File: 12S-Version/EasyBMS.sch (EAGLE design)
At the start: 146 parts, among them IC1 LTC6811IG-2#PBF, Q10 BSS84LT1G, Q11 BSS84LT1G, Q12 BSS84LT1G, Q13 BSS84LT1G, Q2 BSS84LT1G, Q3 BSS84LT1G, Q4 BSS84LT1G, Q5 BSS84LT1G, Q6 BSS84LT1G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

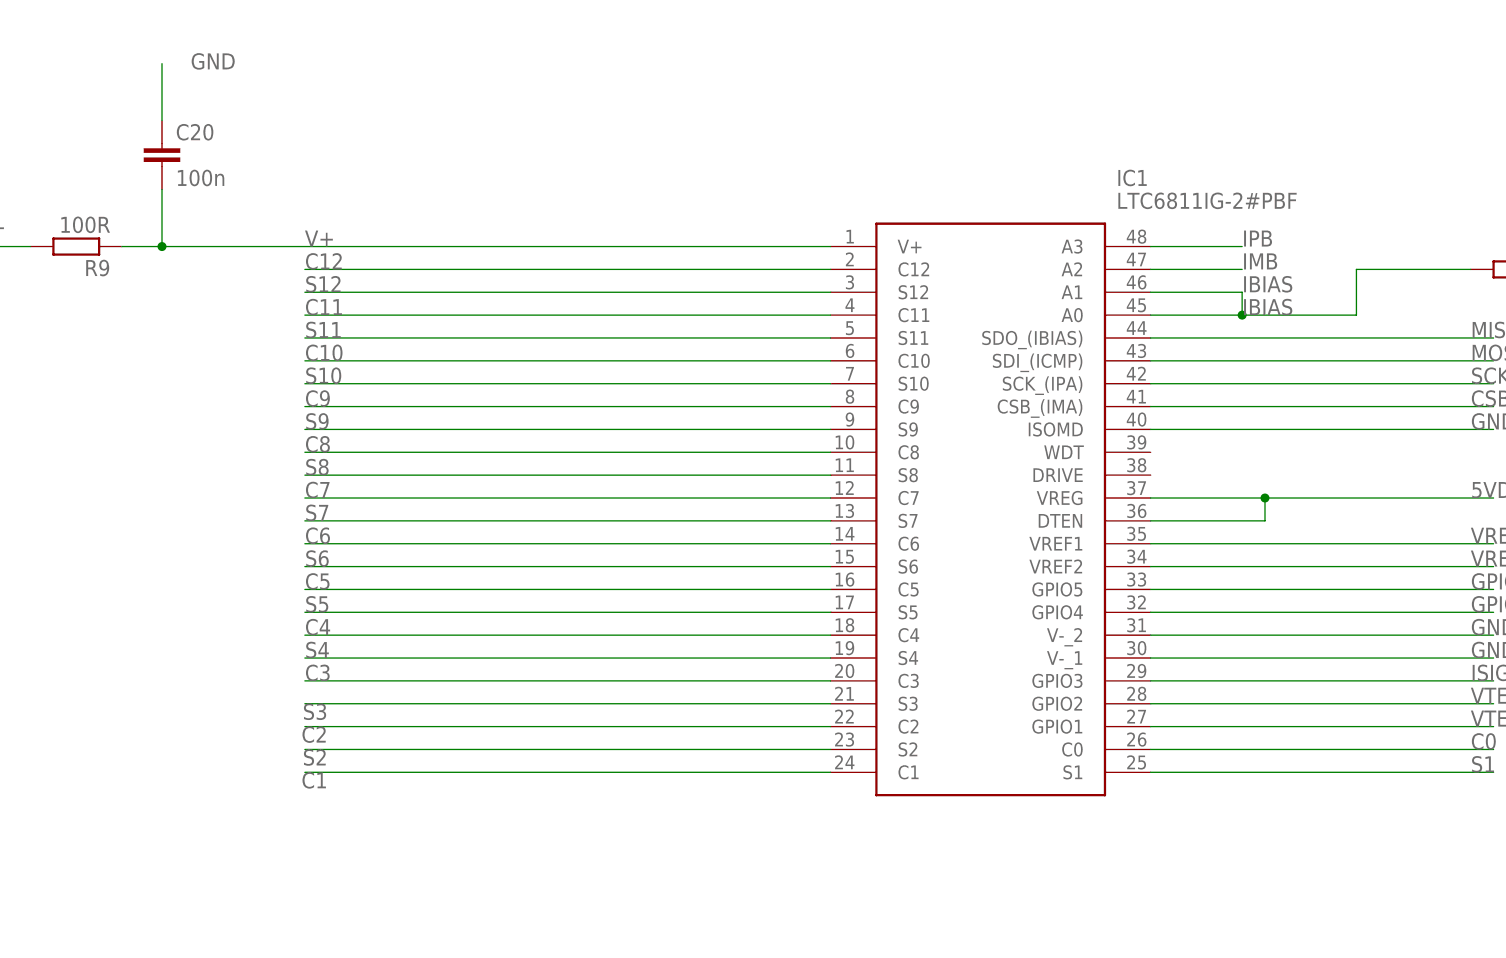
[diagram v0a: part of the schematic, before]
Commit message: symbol of 6811-1 replaced to a original -1 symbol
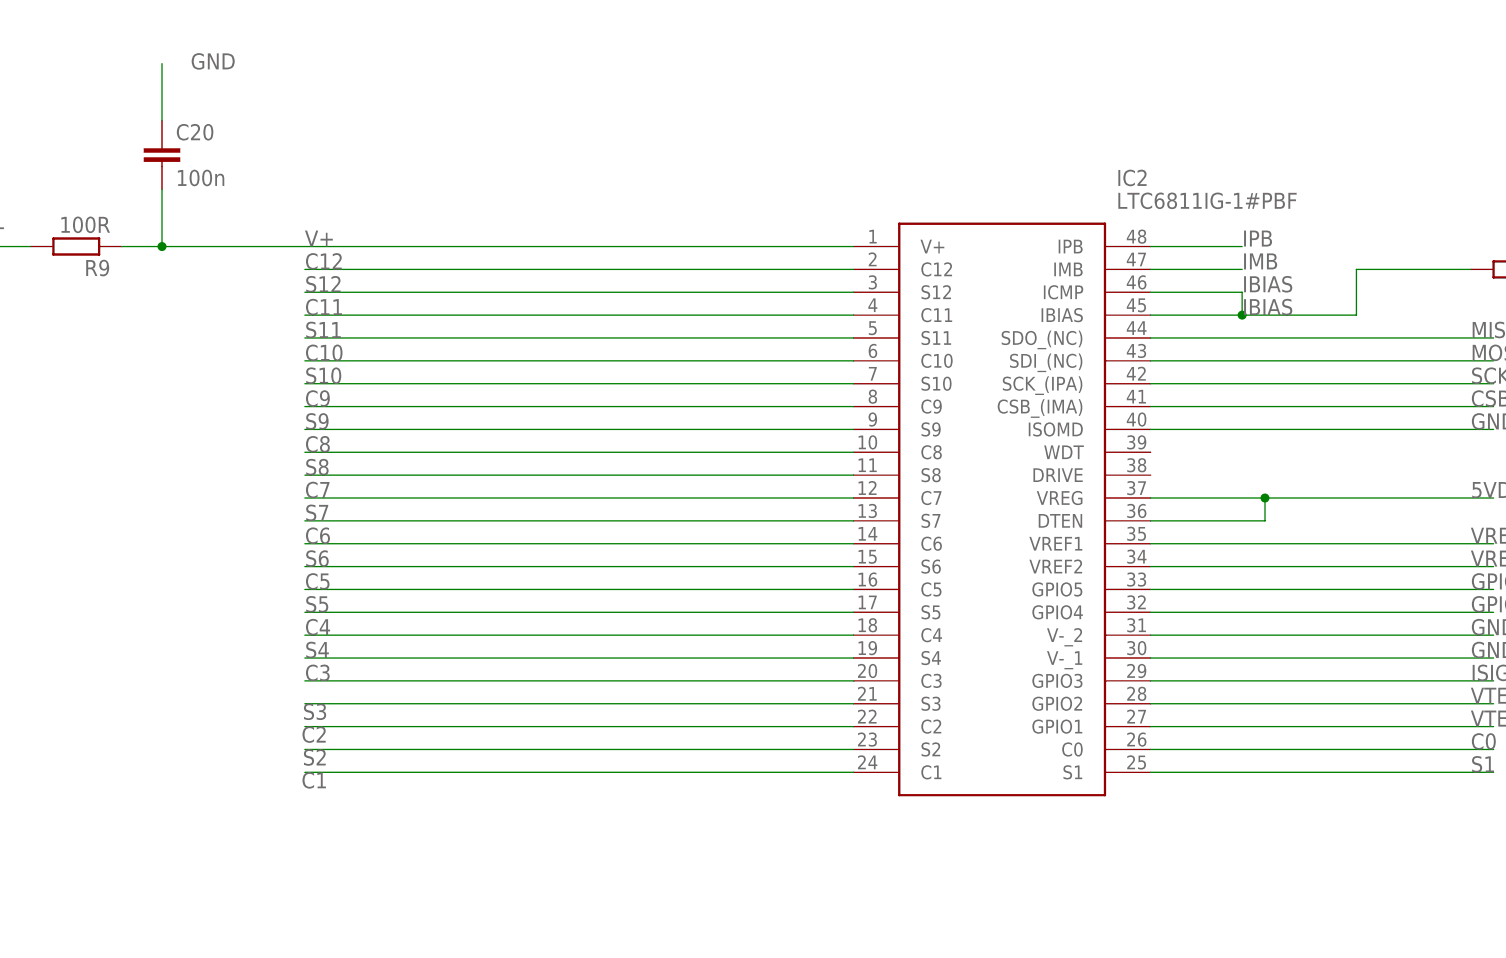
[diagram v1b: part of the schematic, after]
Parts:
- removed IC1: LTC6811IG-2#PBF, SamacSys_Parts:LTC6811IG-2#PBF
- added IC2: LTC6811IG-1#PBF, SamacSys_Parts:LTC6811IG-1#PBF
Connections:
- net 5VDC: now also IC2.DTEN, IC2.VREG; no longer IC1.DTEN, IC1.VREG
- net C0: now also IC2.C0; no longer IC1.C0
- net C1: now also IC2.C1; no longer IC1.C1
- net C10: now also IC2.C10; no longer IC1.C10
- net C11: now also IC2.C11; no longer IC1.C11
- net C12: now also IC2.C12; no longer IC1.C12
- net C2: now also IC2.C2; no longer IC1.C2
- net C3: now also IC2.C3; no longer IC1.C3
- net C4: now also IC2.C4; no longer IC1.C4
- net C5: now also IC2.C5; no longer IC1.C5
- net C6: now also IC2.C6; no longer IC1.C6
- net C7: now also IC2.C7; no longer IC1.C7
- net C8: now also IC2.C8; no longer IC1.C8
- net C9: now also IC2.C9; no longer IC1.C9
- net CSB: now also IC2.CSB_(IMA); no longer IC1.CSB_(IMA)
- net GND: now also IC2.ISOMD, IC2.V-_1, IC2.V-_2; no longer IC1.ISOMD, IC1.V-_1, IC1.V-_2
- net GPIO4: now also IC2.GPIO4; no longer IC1.GPIO4
- net GPIO5: now also IC2.GPIO5; no longer IC1.GPIO5
- net IBIAS: now also IC2.IBIAS, IC2.ICMP; no longer IC1.A0, IC1.A1
- net IMB: now also IC2.IMB; no longer IC1.A2
- net IPB: now also IC2.IPB; no longer IC1.A3
- net ISIGNAL: now also IC2.GPIO3; no longer IC1.GPIO3
- net MISO: now also IC2.SDO_(NC); no longer IC1.SDO_(IBIAS)
- net MOSI: now also IC2.SDI_(NC); no longer IC1.SDI_(ICMP)
- net S1: now also IC2.S1; no longer IC1.S1
- net S10: now also IC2.S10; no longer IC1.S10
- net S11: now also IC2.S11; no longer IC1.S11
- net S12: now also IC2.S12; no longer IC1.S12
- net S2: now also IC2.S2; no longer IC1.S2
- net S3: now also IC2.S3; no longer IC1.S3
- net S4: now also IC2.S4; no longer IC1.S4
- net S5: now also IC2.S5; no longer IC1.S5
- net S6: now also IC2.S6; no longer IC1.S6
- net S7: now also IC2.S7; no longer IC1.S7
- net S8: now also IC2.S8; no longer IC1.S8
- net S9: now also IC2.S9; no longer IC1.S9
- net SCK: now also IC2.SCK_(IPA); no longer IC1.SCK_(IPA)
- net V+: now also IC2.V+; no longer IC1.V+
- net VREF1: now also IC2.VREF1; no longer IC1.VREF1
- net VREF2: now also IC2.VREF2; no longer IC1.VREF2
- net VTEMP1: now also IC2.GPIO1; no longer IC1.GPIO1
- net VTEMP2: now also IC2.GPIO2; no longer IC1.GPIO2

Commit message: add schematic for dc converter design
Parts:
- removed U$1: DC-DC-STEP-DOWN-LM2596HVS, diy-modules:DC-DC-STEP-DOWN-LM2596HVS
- added C18, C21: 100n, rcl:C-EUC0402
- added C2, C23: C249880, rcl:CPOL-EUUD-8X10
- added C22: 1uF, rcl:C-EUC1206
- added C3: C249836, rcl:CPOL-EUUD-10X10
- added D1, D2: C16015, diode:DIODE-DO214BA
- added IC1: LM2596S-5.0_NOPB, SamacSys_Parts:LM2596S-5.0_NOPB
- added L1: C2929443, SamacSys_Parts:CY75-100UH
- added R18: C1017, rcl:R-EU_R0805
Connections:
- new net +5V: C19.1, C22.1, C23.+, IC2.DTEN, IC2.VREG, R18.2
- new net +5V/1: C2.+, C21.1, D2.A, IC1.FB, L1.2, R18.1
- new net N$17: D1.C, IC1.OUT, L1.1
- new net N$25: D2.C, U$2.5V
- net 5VDC: no longer C19.1, IC2.DTEN, IC2.VREG, U$1.OUT+, U$2.5V
- net C12+: now also C18.1, C3.+, IC1.VIN; no longer U$1.IN+
- net GND: now also C18.2, C2.-, C21.2, C22.2, C23.-, C3.-, D1.A, IC1.!ON!/OFF, IC1.GND_1, IC1.GND_2; no longer U$1.IN-, U$1.OUT-
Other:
- moved on the sheet: C1, C19, C20, C4, JP3, LED1, LED2, LED3, LED4, R1, R15, R16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

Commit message: new parts placed inside of the board for a first cost estimation on jlc
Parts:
- IC1: JLCPART (none) -> C347445
- L1: JLCPART (none) -> C2929443
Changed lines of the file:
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@@
 <setting verticaltext="up"/>
 </settings>
-<grid distance="0.025" unitdist="inch" unit="inch" style="lines" multiple="1" display="no" altdistance="0.01" altunitdist="inch" altunit="inch"/>
+<grid distance="0.1" unitdist="inch" unit="inch" style="lines" multiple="1" display="no" altdistance="0.01" altunitdist="inch" altunit="inch"/>
 <layers>
 <layer number="1" name="Top" color="4" fill="1" visible="no" active="no"/>
@@
 <part name="R17" library="rcl" library_urn="urn:adsk.eagle:library:334" deviceset="R-EU_" device="R0603" package3d_urn="urn:adsk.eagle:package:23555/2" value="20k"/>
 <part name="IC2" library="SamacSys_Parts" deviceset="LTC6811IG-1#PBF" device=""/>
-<part name="IC1" library="SamacSys_Parts" deviceset="LM2596S-5.0_NOPB" device=""/>
+<part name="IC1" library="SamacSys_Parts" deviceset="LM2596S-5.0_NOPB" device="">
+<attribute name="JLCPART" value="C347445"/>
+</part>
 <part name="D1" library="diode" library_urn="urn:adsk.eagle:library:210" deviceset="DIODE-" device="DO214BA" package3d_urn="urn:adsk.eagle:package:43453/2" value="C16015"/>
 <part name="GND1" library="supply1" library_urn="urn:adsk.eagle:library:371" deviceset="GND" device=""/>
@@
 <part name="GND6" library="supply1" library_urn="urn:adsk.eagle:library:371" deviceset="GND" device=""/>
 <part name="GND7" library="supply1" library_urn="urn:adsk.eagle:library:371" deviceset="GND" device=""/>
-<part name="L1" library="SamacSys_Parts" deviceset="CY75-100UH" device="" value="C2929443"/>
+<part name="L1" library="SamacSys_Parts" deviceset="CY75-100UH" device="" value="C2929443">
+<attribute name="JLCPART" value="C2929443"/>
+</part>
 <part name="C2" library="rcl" library_urn="urn:adsk.eagle:library:334" deviceset="CPOL-EU" device="UD-8X10" package3d_urn="urn:adsk.eagle:package:23473/1" value="C249880"/>
 <part name="C3" library="rcl" library_urn="urn:adsk.eagle:library:334" deviceset="CPOL-EU" device="UD-10X10" package3d_urn="urn:adsk.eagle:package:23469/1" value="C249836"/>
@@
 <attribute name="NAME" x="29.21" y="383.54" size="1.778" layer="95" rot="R180" align="center-left"/>
 <attribute name="VALUE" x="39.37" y="386.08" size="1.778" layer="96" rot="R180" align="center-left"/>
+<attribute name="JLCPART" x="45.72" y="391.16" size="1.778" layer="96" rot="R180"/>
 </instance>
 <instance part="D1" gate="G$1" x="53.34" y="388.62" smashed="yes" rot="R90">
@@
 <attribute name="NAME" x="59.69" y="395.986" size="1.778" layer="95"/>
 <attribute name="VALUE" x="59.563" y="390.652" size="1.778" layer="96"/>
+<attribute name="JLCPART" x="63.5" y="398.78" size="1.778" layer="96"/>
 </instance>
 <instance part="C2" gate="G$1" x="78.74" y="388.62" smashed="yes">

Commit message: layout with integrated dc/dc is ready, changed input capacitor to a larger one
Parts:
- removed C3: C249836, rcl:CPOL-EUUD-10X10
- added C24: C249935, SamacSys_Parts:VZH471M1JTR-1616
- C21: value 100n -> 1uF; device rcl:C-EUC0402 -> rcl:C-EUC1206
- D1, D2: device diode:DIODE-DO214BA -> diode:DIODE-DO214AC
- IC1: JLCPART C347445 -> (none)
- L1: JLCPART C2929443 -> (none)
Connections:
- removed net 5VDC: JP9.1, JP9.2
- net +5V: now also JP9.1, JP9.2
- net C12+: now also C24.+; no longer C3.+
- net GND: now also C24.-; no longer C3.-
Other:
- moved on the sheet: IC1

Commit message: moved some parts a bit to solve collisions
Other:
- moved on the sheet: IC1

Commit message: added 100R in serial of DCDC input to limit rush in current, separate V+ wires used
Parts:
- added R19: 100R, rcl:R-EU_R1206
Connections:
- new net C12+POWER: JP7.2_CTOTAL+, R19.2
- new net GND2: LED1.C, LED2.C, LED3.C, LED4.C, U$2.GND
- new net N$75: C18.1, C24.+, IC1.VIN, R19.1
- net C12+: no longer C18.1, C24.+, IC1.VIN, JP7.2_CTOTAL+
- net GND: no longer LED1.C, LED2.C, LED3.C, LED4.C, U$2.GND
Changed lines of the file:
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@@
 <part name="C24" library="SamacSys_Parts" deviceset="VZH471M1JTR-1616" device="" package3d_urn="urn:adsk.eagle:package:18353981/3" value="C249935"/>
 <part name="P+2" library="supply1" library_urn="urn:adsk.eagle:library:371" deviceset="+5V" device=""/>
+<part name="R19" library="rcl" library_urn="urn:adsk.eagle:library:334" deviceset="R-EU_" device="R1206" package3d_urn="urn:adsk.eagle:package:23540/2" value="100R"/>
 </parts>
 <sheets>
@@
 <attribute name="VALUE" x="-80.01" y="403.86" size="1.778" layer="96" rot="R90"/>
 </instance>
+<instance part="R19" gate="G$1" x="50.8" y="427.355" smashed="yes" rot="R90">
+<attribute name="NAME" x="49.3014" y="423.545" size="1.778" layer="95" rot="R90"/>
+<attribute name="VALUE" x="54.102" y="423.545" size="1.778" layer="96" rot="R90"/>
+</instance>
 </instances>
 <busses>
@@
 <net name="GND" class="0">
 <segment>
-<wire x1="78.105" y1="267.335" x2="62.23" y2="267.335" width="0.1524" layer="91"/>
+<pinref part="GND4" gate="1" pin="GND"/>
+<pinref part="C19" gate="G$1" pin="2"/>
+<wire x1="62.23" y1="272.415" x2="62.23" y2="267.335" width="0.1524" layer="91"/>
 <wire x1="62.23" y1="267.335" x2="46.99" y2="267.335" width="0.1524" layer="91"/>
-<wire x1="46.99" y1="267.335" x2="31.75" y2="267.335" width="0.1524" layer="91"/>
-<pinref part="U$2" gate="G$1" pin="GND"/>
-<wire x1="78.105" y1="307.975" x2="29.21" y2="307.975" width="0.1524" layer="91"/>
-<wire x1="78.105" y1="307.975" x2="78.105" y2="267.335" width="0.1524" layer="91"/>
-<wire x1="31.75" y1="272.415" x2="31.75" y2="267.335" width="0.1524" layer="91"/>
+<pinref part="C1" gate="G$1" pin="2"/>
 <wire x1="46.99" y1="272.415" x2="46.99" y2="267.335" width="0.1524" layer="91"/>
 <junction x="46.99" y="267.335"/>
-<wire x1="62.23" y1="272.415" x2="62.23" y2="267.335" width="0.1524" layer="91"/>
-<junction x="62.23" y="267.335"/>
+<wire x1="46.99" y1="267.335" x2="46.99" y2="262.255" width="0.1524" layer="91"/>
+<wire x1="46.99" y1="267.335" x2="31.75" y2="267.335" width="0.1524" layer="91"/>
 <pinref part="C4" gate="G$1" pin="2"/>
-<pinref part="C19" gate="G$1" pin="2"/>
-<pinref part="C1" gate="G$1" pin="2"/>
-<pinref part="GND4" gate="1" pin="GND"/>
-<wire x1="46.99" y1="267.335" x2="46.99" y2="262.255" width="0.1524" layer="91"/>
-<pinref part="LED2" gate="G$1" pin="C"/>
-<pinref part="LED1" gate="G$1" pin="C"/>
-<wire x1="74.93" y1="346.075" x2="78.105" y2="346.075" width="0.1524" layer="91"/>
-<wire x1="78.105" y1="346.075" x2="78.105" y2="335.915" width="0.1524" layer="91"/>
-<wire x1="78.105" y1="335.915" x2="74.93" y2="335.915" width="0.1524" layer="91"/>
-<pinref part="LED3" gate="G$1" pin="C"/>
-<wire x1="78.105" y1="335.915" x2="78.105" y2="325.755" width="0.1524" layer="91"/>
-<wire x1="78.105" y1="325.755" x2="74.93" y2="325.755" width="0.1524" layer="91"/>
-<junction x="78.105" y="335.915"/>
-<pinref part="LED4" gate="G$1" pin="C"/>
-<wire x1="78.105" y1="325.755" x2="78.105" y2="315.595" width="0.1524" layer="91"/>
-<wire x1="78.105" y1="315.595" x2="74.93" y2="315.595" width="0.1524" layer="91"/>
-<junction x="78.105" y="325.755"/>
-<wire x1="78.105" y1="315.595" x2="78.105" y2="307.975" width="0.1524" layer="91"/>
-<junction x="78.105" y="315.595"/>
-<junction x="78.105" y="307.975"/>
+<wire x1="31.75" y1="272.415" x2="31.75" y2="267.335" width="0.1524" layer="91"/>
 </segment>
 <segment>
@@
 <net name="C12+" class="0">
 <segment>
-<pinref part="JP7" gate="G$1" pin="2_CTOTAL+"/>
-<wire x1="162.56" y1="515.62" x2="180.34" y2="515.62" width="0.1524" layer="91"/>
-<label x="175.26" y="515.62" size="1.778" layer="95"/>
-</segment>
-<segment>
 <wire x1="-355.6" y1="637.54" x2="-365.76" y2="637.54" width="0.1524" layer="91"/>
 <pinref part="Q13" gate="G$1" pin="S"/>
@@
 </segment>
 <segment>
+<pinref part="R15" gate="G$1" pin="2"/>
+<wire x1="-24.13" y1="368.935" x2="-24.13" y2="371.475" width="0.1524" layer="91"/>
+<label x="-24.13" y="371.475" size="1.778" layer="95"/>
+</segment>
+<segment>
+<pinref part="R9" gate="G$1" pin="2"/>
+<wire x1="-114.3" y1="510.54" x2="-125.73" y2="510.54" width="0.1524" layer="91"/>
+<label x="-123.19" y="511.81" size="1.778" layer="95"/>
+</segment>
+<segment>
 <pinref part="JP7" gate="G$1" pin="1_TOTAL+"/>
 <wire x1="154.94" y1="515.62" x2="132.08" y2="515.62" width="0.1524" layer="91"/>
 <label x="127" y="515.62" size="1.778" layer="95"/>
-</segment>
-<segment>
-<label x="60.96" y="422.91" size="1.778" layer="95"/>
-<pinref part="IC1" gate="G$1" pin="VIN"/>
-<wire x1="67.31" y1="421.64" x2="57.785" y2="421.64" width="0.1524" layer="91"/>
-<wire x1="57.785" y1="421.64" x2="50.8" y2="421.64" width="0.1524" layer="91"/>
-<wire x1="45.72" y1="391.16" x2="50.8" y2="391.16" width="0.1524" layer="91"/>
-<wire x1="50.8" y1="391.16" x2="50.8" y2="421.64" width="0.1524" layer="91"/>
-<pinref part="C18" gate="G$1" pin="1"/>
-<wire x1="57.785" y1="419.735" x2="57.785" y2="421.64" width="0.1524" layer="91"/>
-<junction x="57.785" y="421.64"/>
-<wire x1="67.31" y1="419.735" x2="67.31" y2="421.64" width="0.1524" layer="91"/>
-<pinref part="C24" gate="G$1" pin="+"/>
-</segment>
-<segment>
-<pinref part="R15" gate="G$1" pin="2"/>
-<wire x1="-24.13" y1="368.935" x2="-24.13" y2="371.475" width="0.1524" layer="91"/>
-<label x="-24.13" y="371.475" size="1.778" layer="95"/>
-</segment>
-<segment>
-<pinref part="R9" gate="G$1" pin="2"/>
-<wire x1="-114.3" y1="510.54" x2="-125.73" y2="510.54" width="0.1524" layer="91"/>
-<label x="-123.19" y="511.81" size="1.778" layer="95"/>
 </segment>
 </net>
@@
 </segment>
 </net>
+<net name="C12+POWER" class="0">
+<segment>
+<pinref part="JP7" gate="G$1" pin="2_CTOTAL+"/>
+<wire x1="162.56" y1="515.62" x2="180.34" y2="515.62" width="0.1524" layer="91"/>
+<label x="175.26" y="515.62" size="1.778" layer="95"/>
+</segment>
+<segment>
+<pinref part="R19" gate="G$1" pin="2"/>
+<wire x1="50.8" y1="432.435" x2="50.8" y2="437.515" width="0.1524" layer="91"/>
+<label x="38.735" y="438.785" size="1.778" layer="95"/>
+</segment>
+</net>
+<net name="N$75" class="0">
+<segment>
+<pinref part="IC1" gate="G$1" pin="VIN"/>
+<pinref part="R19" gate="G$1" pin="1"/>
+<wire x1="45.72" y1="391.16" x2="50.8" y2="391.16" width="0.1524" layer="91"/>
+<wire x1="50.8" y1="391.16" x2="50.8" y2="422.275" width="0.1524" layer="91"/>
+<wire x1="50.8" y1="422.275" x2="57.785" y2="422.275" width="0.1524" layer="91"/>
+<junction x="50.8" y="422.275"/>
+<pinref part="C18" gate="G$1" pin="1"/>
+<wire x1="57.785" y1="422.275" x2="57.785" y2="419.735" width="0.1524" layer="91"/>
+<pinref part="C24" gate="G$1" pin="+"/>
+<wire x1="57.785" y1="422.275" x2="67.31" y2="422.275" width="0.1524" layer="91"/>
+<wire x1="67.31" y1="422.275" x2="67.31" y2="419.735" width="0.1524" layer="91"/>
+<junction x="57.785" y="422.275"/>
+</segment>
+</net>
+<net name="GND2" class="0">
+<segment>
+<pinref part="U$2" gate="G$1" pin="GND"/>
+<wire x1="78.105" y1="307.975" x2="29.21" y2="307.975" width="0.1524" layer="91"/>
+<pinref part="LED2" gate="G$1" pin="C"/>
+<pinref part="LED1" gate="G$1" pin="C"/>
+<wire x1="74.93" y1="346.075" x2="78.105" y2="346.075" width="0.1524" layer="91"/>
+<wire x1="78.105" y1="346.075" x2="78.105" y2="335.915" width="0.1524" layer="91"/>
+<wire x1="78.105" y1="335.915" x2="74.93" y2="335.915" width="0.1524" layer="91"/>
+<pinref part="LED3" gate="G$1" pin="C"/>
+<wire x1="78.105" y1="335.915" x2="78.105" y2="325.755" width="0.1524" layer="91"/>
+<wire x1="78.105" y1="325.755" x2="74.93" y2="325.755" width="0.1524" layer="91"/>
+<junction x="78.105" y="335.915"/>
+<pinref part="LED4" gate="G$1" pin="C"/>
+<wire x1="78.105" y1="325.755" x2="78.105" y2="315.595" width="0.1524" layer="91"/>
+<wire x1="78.105" y1="315.595" x2="74.93" y2="315.595" width="0.1524" layer="91"/>
+<junction x="78.105" y="325.755"/>
+<wire x1="78.105" y1="315.595" x2="78.105" y2="307.975" width="0.1524" layer="91"/>
+<junction x="78.105" y="315.595"/>
+<label x="75.565" y="305.435" size="1.778" layer="95"/>
+</segment>
+</net>
